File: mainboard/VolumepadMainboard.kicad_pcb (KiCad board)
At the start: 2 copper layers, 112 x 78 mm, 158 parts, among them J1 USB_C_Receptacle_USB2.0, J2 BLDC, J3 USB_Extension_Board, J4 Touch_Extension_Board, Q1 MMBT4403, Q2 2N7002, SW1 SW_Push, SW2 SW_Push, SW3 SW_Push, SW4 SW_Push, U1 ESP32-S3-WROOM-1, U2 AP2114HA-3.3, U3 MT6701-CT, U4 HX711, U5 TMC6300, U6 USB6B1, U7 SN74LV1T34DBV

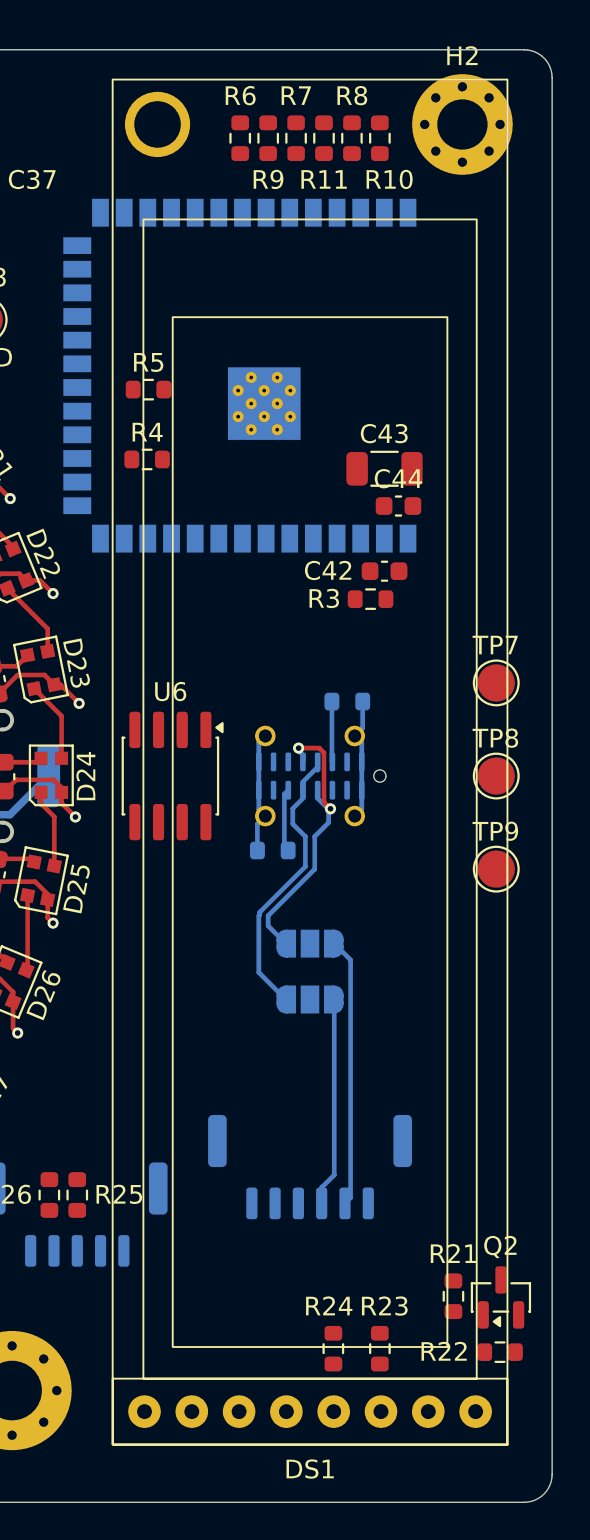
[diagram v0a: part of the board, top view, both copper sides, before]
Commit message: Removed the onboard USB-C plug and added a display connector
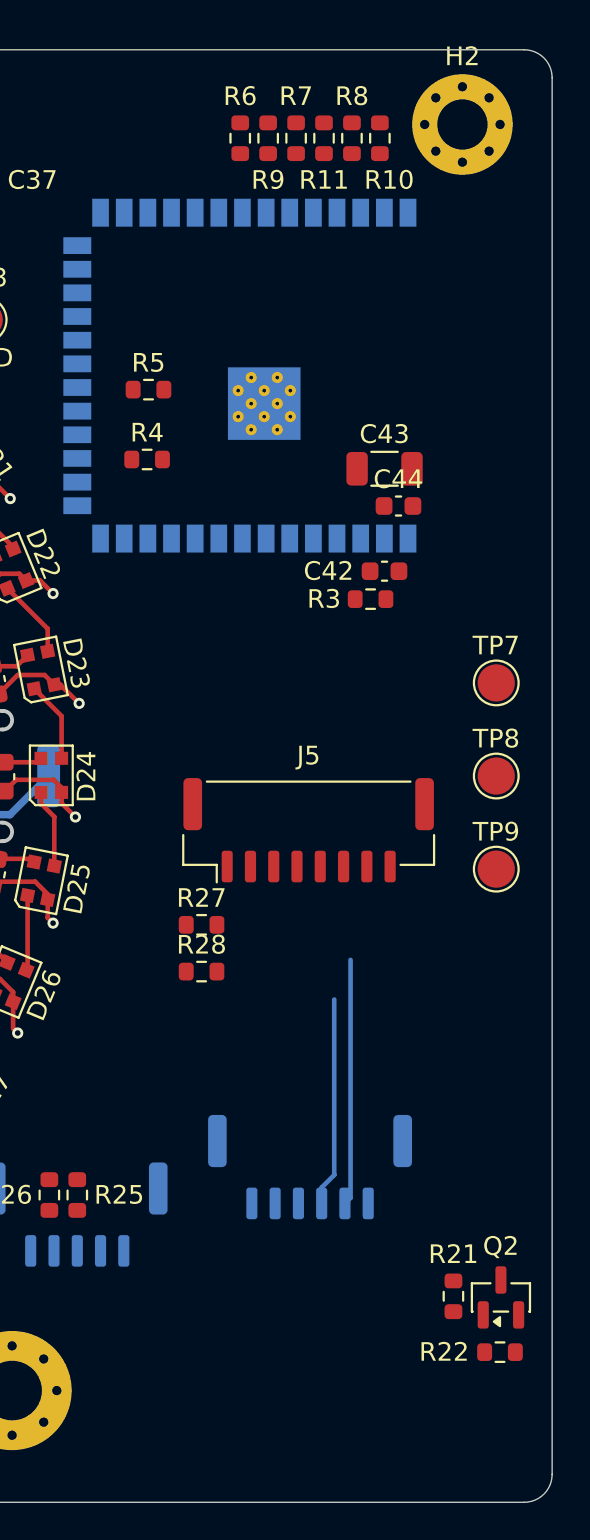
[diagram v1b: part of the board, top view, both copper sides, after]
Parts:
- removed DS1: TFT_2.25_ST7789, PhiMai:TFT_2.25_ST7789_1x08_2.54mm
- removed J1: USB_C_Receptacle_USB2.0, Connector_USB:USB_C_Receptacle_G-Switch_GT-USB-7051x
- removed JP1: Jumper_USB_D+, Jumper:SolderJumper-3_P1.3mm_Open_RoundedPad1.0x1.5mm_NumberLabels
- removed JP2: Jumper_USB_D-, Jumper:SolderJumper-3_P1.3mm_Open_RoundedPad1.0x1.5mm_NumberLabels
- removed R1, R2: 5.1k, Resistor_SMD:R_0603_1608Metric
- removed R23, R24: 33, Resistor_SMD:R_0603_1608Metric
- removed U6: USB6B1, Package_SO:SOIC-8_3.9x4.9mm_P1.27mm
- added J5: Display_Connector, Connector_JST:JST_GH_BM08B-GHS-TBT_1x08-1MP_P1.25mm_Vertical, F.Cu at (142.9, 102.9)
- added R27: 33, Resistor_SMD:R_0603_1608Metric, F.Cu at (137.2, 108.0)
- added R28: 33, Resistor_SMD:R_0603_1608Metric, F.Cu at (137.2, 110.5)
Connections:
- J3 pad 1: GND -> +5V
- J3 pad 2: Aux_USB_D- -> +5V
- J3 pad 3: Aux_USB_D+ -> GND
- J3 pad 4: +5V -> Aux_USB_D-
- J3 pad 5: GND -> Aux_USB_D+
- J3 pad 6: +5V -> GND
- U1 pad 13: Protected_USB_D- -> Aux_USB_D-
- U1 pad 14: Protected_USB_D+ -> Aux_USB_D+
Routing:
- net Onboard_USB_D-: track 15.8 -> 0.00 mm, vias 2 -> 0
- net Onboard_USB_D+: track 15.7 -> 0.00 mm
- net Aux_USB_D-: track 14.4 -> 0.00 mm
- net +5V: track 66.1 -> 79.3 mm
- net Aux_USB_D+: track 11.2 -> 0.00 mm
- net /USB_CC2: track 3.41 -> 0.00 mm
- net /USB_CC1: track 3.25 -> 0.00 mm
- net GND: track 191.5 -> 189.5 mm

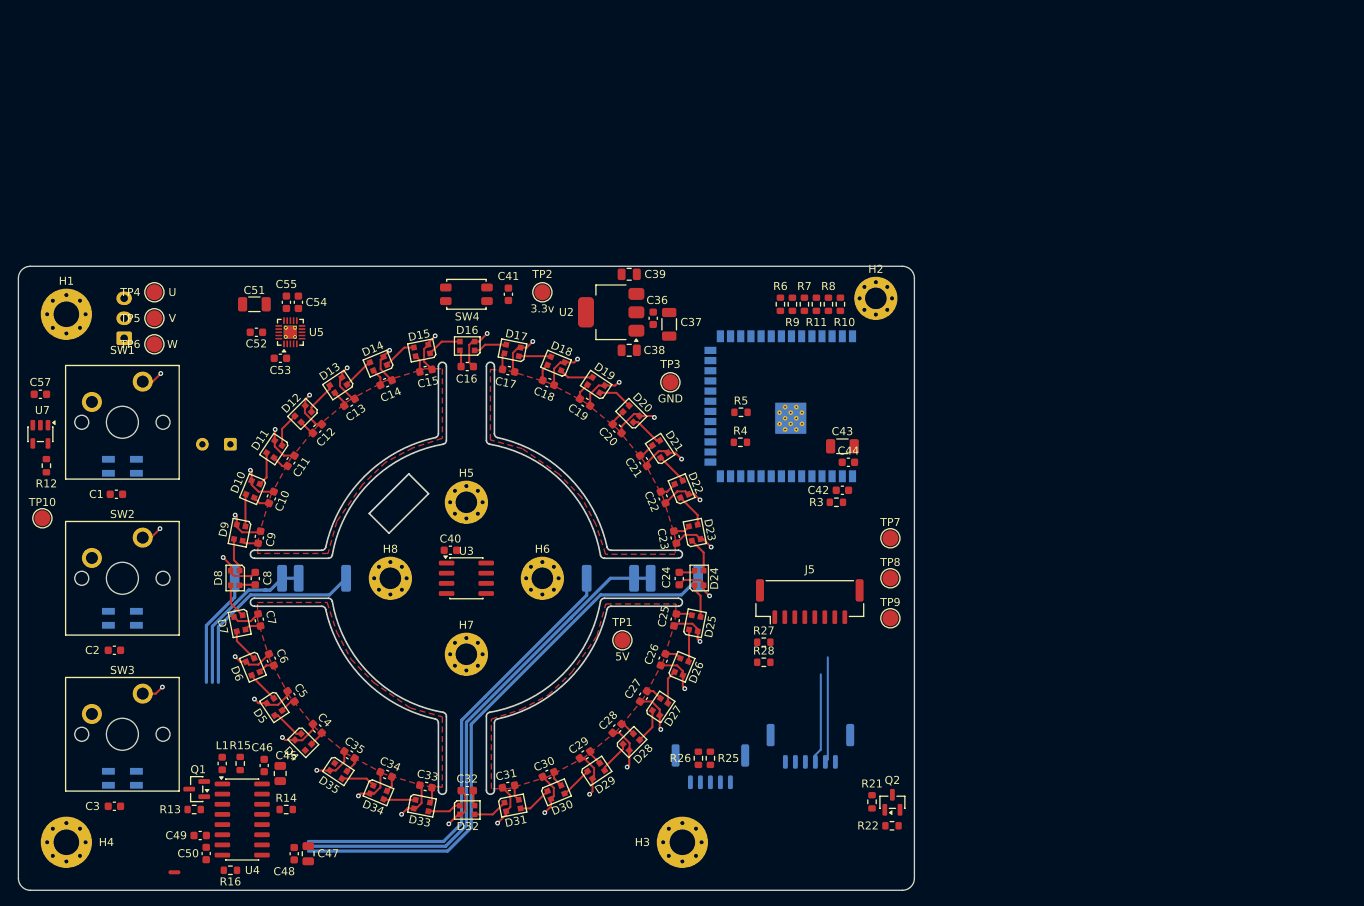
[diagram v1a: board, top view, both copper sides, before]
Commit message: Rearranged LEDs
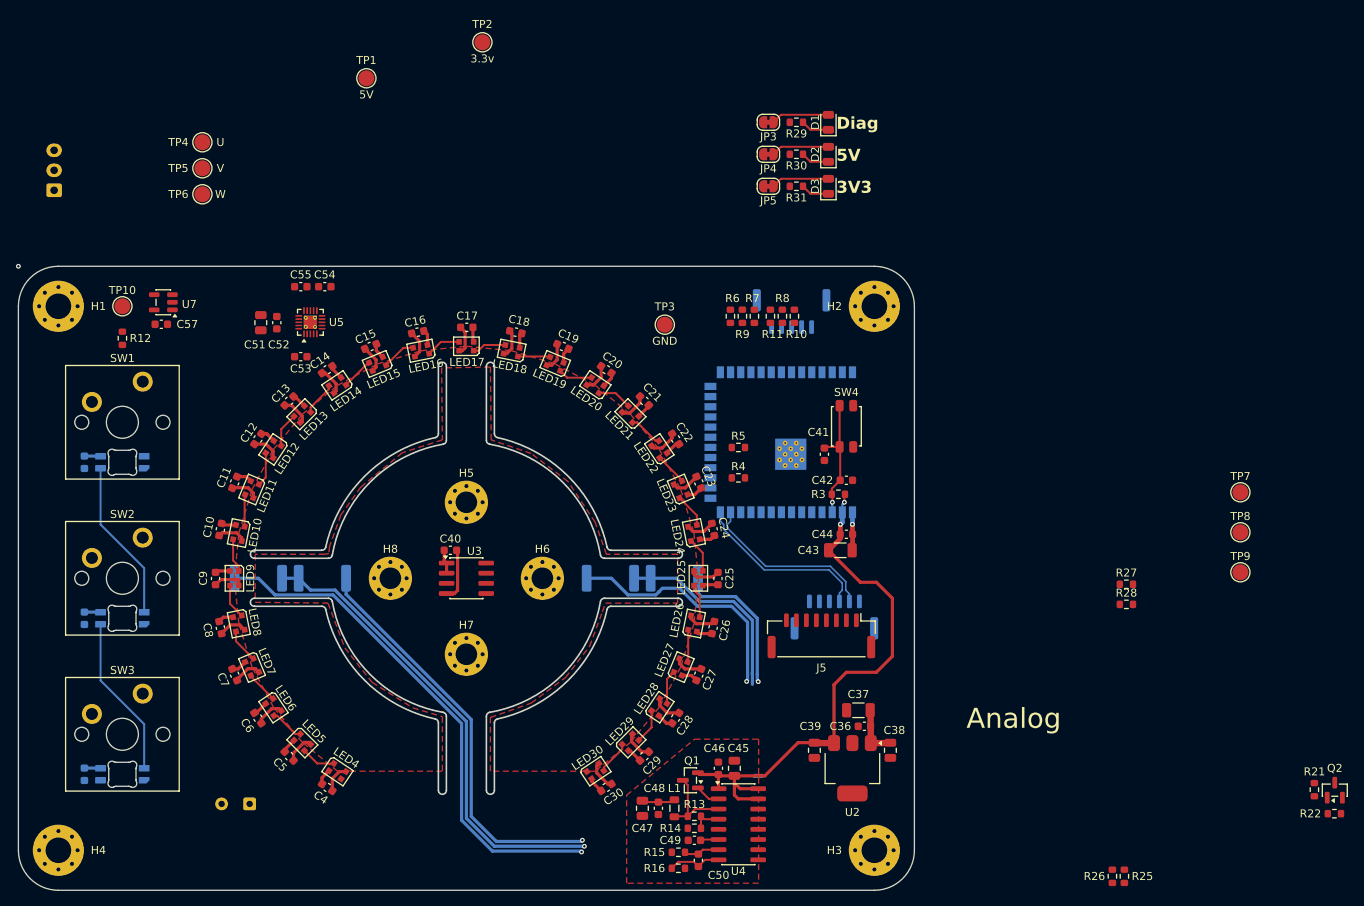
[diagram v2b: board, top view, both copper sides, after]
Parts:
- removed C31, C32, C33, C34, C35: 0.1uF, Capacitor_SMD:C_0603_1608Metric
- removed D10, D11, D12, D13, D14, D15, D16, D17, D18, D19, D20, D21, D22, D23, D24, D25, D26, D27, D28, D29, D30, D31, D32, D33, D34, D35, D4, D5, D6, D7, D8, D9: WS2812B-2020, LED_SMD:LED_WS2812B-2020_PLCC4_2.0x2.0mm
- added JP3: Standby Jumper, Jumper:SolderJumper-2_P1.3mm_Bridged_RoundedPad1.0x1.5mm, F.Cu at (137.8, 43.0)
- added JP4: Standby Jumper, Jumper:SolderJumper-2_P1.3mm_Bridged_RoundedPad1.0x1.5mm, F.Cu at (137.8, 47.0)
- added JP5: Standby Jumper, Jumper:SolderJumper-2_P1.3mm_Bridged_RoundedPad1.0x1.5mm, F.Cu at (137.8, 51.0)
- added LED1: MX_SK6812MINI-E, PCM_marbastlib-mx:LED_MX_6028R, B.Cu at (57.0, 85.5)
- added LED10: WS2812B-2020, PhiMai:LED_WS2812B-2020_PLCC4_2.0x2.0mm, F.Cu at (71.6, 94.3)
- added LED11: WS2812B-2020, PhiMai:LED_WS2812B-2020_PLCC4_2.0x2.0mm, F.Cu at (73.2, 88.9)
- added LED12: WS2812B-2020, PhiMai:LED_WS2812B-2020_PLCC4_2.0x2.0mm, F.Cu at (75.9, 83.9)
- added LED13: WS2812B-2020, PhiMai:LED_WS2812B-2020_PLCC4_2.0x2.0mm, F.Cu at (79.5, 79.5)
- added LED14: WS2812B-2020, PhiMai:LED_WS2812B-2020_PLCC4_2.0x2.0mm, F.Cu at (83.9, 75.9)
- added LED15: WS2812B-2020, PhiMai:LED_WS2812B-2020_PLCC4_2.0x2.0mm, F.Cu at (88.9, 73.2)
- added LED16: WS2812B-2020, PhiMai:LED_WS2812B-2020_PLCC4_2.0x2.0mm, F.Cu at (94.3, 71.6)
- added LED17: WS2812B-2020, PhiMai:LED_WS2812B-2020_PLCC4_2.0x2.0mm, F.Cu at (100.0, 71.0)
- added LED18: WS2812B-2020, PhiMai:LED_WS2812B-2020_PLCC4_2.0x2.0mm, F.Cu at (105.7, 71.6)
- added LED19: WS2812B-2020, PhiMai:LED_WS2812B-2020_PLCC4_2.0x2.0mm, F.Cu at (111.1, 73.2)
- added LED2: MX_SK6812MINI-E, PCM_marbastlib-mx:LED_MX_6028R, B.Cu at (57.0, 105.0)
- added LED20: WS2812B-2020, PhiMai:LED_WS2812B-2020_PLCC4_2.0x2.0mm, F.Cu at (116.1, 75.9)
- added LED21: WS2812B-2020, PhiMai:LED_WS2812B-2020_PLCC4_2.0x2.0mm, F.Cu at (120.5, 79.5)
- added LED22: WS2812B-2020, PhiMai:LED_WS2812B-2020_PLCC4_2.0x2.0mm, F.Cu at (124.1, 83.9)
- added LED23: WS2812B-2020, PhiMai:LED_WS2812B-2020_PLCC4_2.0x2.0mm, F.Cu at (126.8, 88.9)
- added LED24: WS2812B-2020, PhiMai:LED_WS2812B-2020_PLCC4_2.0x2.0mm, F.Cu at (128.4, 94.3)
- added LED25: WS2812B-2020, PhiMai:LED_WS2812B-2020_PLCC4_2.0x2.0mm, F.Cu at (129.0, 100.0)
- added LED26: WS2812B-2020, PhiMai:LED_WS2812B-2020_PLCC4_2.0x2.0mm, F.Cu at (128.4, 105.7)
- added LED27: WS2812B-2020, PhiMai:LED_WS2812B-2020_PLCC4_2.0x2.0mm, F.Cu at (126.8, 111.1)
- added LED28: WS2812B-2020, PhiMai:LED_WS2812B-2020_PLCC4_2.0x2.0mm, F.Cu at (124.1, 116.1)
- added LED29: WS2812B-2020, PhiMai:LED_WS2812B-2020_PLCC4_2.0x2.0mm, F.Cu at (120.5, 120.5)
- added LED3: MX_SK6812MINI-E, PCM_marbastlib-mx:LED_MX_6028R, B.Cu at (57.0, 124.5)
- added LED30: WS2812B-2020, PhiMai:LED_WS2812B-2020_PLCC4_2.0x2.0mm, F.Cu at (116.1, 124.1)
- added LED4: WS2812B-2020, PhiMai:LED_WS2812B-2020_PLCC4_2.0x2.0mm, F.Cu at (83.9, 124.1)
- added LED5: WS2812B-2020, PhiMai:LED_WS2812B-2020_PLCC4_2.0x2.0mm, F.Cu at (79.5, 120.5)
- added LED6: WS2812B-2020, PhiMai:LED_WS2812B-2020_PLCC4_2.0x2.0mm, F.Cu at (75.9, 116.1)
- added LED7: WS2812B-2020, PhiMai:LED_WS2812B-2020_PLCC4_2.0x2.0mm, F.Cu at (73.2, 111.1)
- added LED8: WS2812B-2020, PhiMai:LED_WS2812B-2020_PLCC4_2.0x2.0mm, F.Cu at (71.6, 105.7)
- added LED9: WS2812B-2020, PhiMai:LED_WS2812B-2020_PLCC4_2.0x2.0mm, F.Cu at (71.0, 100.0)
- added R29: 330, Resistor_SMD:R_0603_1608Metric, F.Cu at (141.2, 43.0)
- added R30: 2.2k, Resistor_SMD:R_0603_1608Metric, F.Cu at (141.2, 47.0)
- added R31: 1k, Resistor_SMD:R_0603_1608Metric, F.Cu at (141.2, 51.0)
- C1, C2, C3, NT1: moved to B.Cu
- C51: footprint Capacitor_SMD:C_1206_3216Metric -> Capacitor_SMD:C_0805_2012Metric
- D1: value SK6812MINI-E -> ORANGE; footprint LED_SMD:LED_SK6812MINI_PLCC4_3.5x3.5mm_P1.75mm -> LED_SMD:LED_0805_2012Metric; moved to F.Cu
- D2: value SK6812MINI-E -> GREEN; footprint LED_SMD:LED_SK6812MINI_PLCC4_3.5x3.5mm_P1.75mm -> LED_SMD:LED_0805_2012Metric; moved to F.Cu
- D3: value SK6812MINI-E -> BLUE; footprint LED_SMD:LED_SK6812MINI_PLCC4_3.5x3.5mm_P1.75mm -> LED_SMD:LED_0805_2012Metric; moved to F.Cu
- H2: footprint MountingHole:MountingHole_2.7mm_M2.5_Pad_Via -> MountingHole:MountingHole_3.2mm_M3_Pad_Via
- L1: footprint Inductor_SMD:L_0603_1608Metric -> Inductor_SMD:L_0805_2012Metric
- moved D3 115.2 mm to (145.2, 51.0), turned to 90 degrees
- moved D2 105.6 mm to (145.2, 47.0), turned to 90 degrees
- moved D1 98.2 mm to (145.2, 43.0), turned to 90 degrees
- moved TP1 77.2 mm to (87.5, 37.5)
- moved NT1 74.0 mm to (136.5, 124.7), turned to 0 degrees
- moved U2 64.5 mm to (148.2, 123.8), turned to -90 degrees
- moved C39 63.8 mm to (143.5, 121.5), turned to -90 degrees
- moved R13 62.5 mm to (128.5, 129.8)
- moved U4 62.0 mm to (134.0, 130.8)
- moved C49 61.8 mm to (128.5, 132.8)
- moved Q1 61.7 mm to (128.0, 125.2)
- moved C50 61.5 mm to (129.0, 135.2)
- moved C38 59.7 mm to (153.0, 121.5), turned to -90 degrees
- moved J4 57.8 mm to (140.7, 66.7)
- moved C36 57.4 mm to (149.8, 118.5), turned to 180 degrees
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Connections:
- net STRAIN_E- renamed GNDA
- D1 pad 1: Net-(D1-DOUT) -> Net-(D1-K)
- D1 pad 2: GND -> Net-(D1-A)
- D2 pad 1: Net-(D2-DOUT) -> Net-(D2-K)
- D2 pad 2: GND -> Net-(D2-A)
- D3 pad 1: LED_DATA_5V_AFTER_KEYS -> Net-(D3-K)
- D3 pad 2: GND -> Net-(D3-A)
- J3 pad 4: Aux_USB_D- -> Aux_USB_D+
- J3 pad 5: Aux_USB_D+ -> Aux_USB_D-
- R12 pad 2: Net-(D1-DIN) -> Net-(LED1-DIN)
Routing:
- net GND: track 189.5 -> 65.1 mm, vias 34 -> 1
- net +3V3: track 0.00 -> 74.2 mm, vias 0 -> 2
- net STRAIN_S+: track 64.4 -> 25.2 mm
- net STRAIN_S-: track 20.5 -> 58.7 mm, vias 0 -> 1
- net +5V: track 79.3 -> 110.9 mm
- net GNDA: track 71.7 -> 95.2 mm, vias 0 -> 2
- net Aux_USB_D-: track 0.00 -> 22.4 mm
- net Aux_USB_D+: track 0.00 -> 22.3 mm
- net STRAIN_E+: track 95.8 -> 74.2 mm, vias 0 -> 2
- net Net-(LED2-DOUT): track 0.00 -> 20.3 mm
- net Net-(LED1-DOUT): track 0.00 -> 20.3 mm
- net ESP32_EN: track 0.00 -> 15.8 mm, vias 0 -> 1
- net Net-(Q1-C): track 0.00 -> 10.7 mm
- net Net-(D3-A): track 0.00 -> 7.24 mm
- net Net-(D2-A): track 0.00 -> 7.24 mm
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- added copper zone on F.Cu, net GNDA
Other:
- outline, holes or cut-outs redrawn
- board text added: "3V3"
- board text added: "5V"
- board text added: "Analog"
- board text added: "Diag"
